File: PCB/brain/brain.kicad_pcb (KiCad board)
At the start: 4 copper layers, 100 x 115 mm, 225 parts, among them J1 Screw_Terminal_01x02, J10 Conn_01x12, J11 Conn_01x04, J12 BAT, J13 Conn_01x05, J14 Conn_01x02, J2 Conn_01x04, J3 RJ45_Hanrun_HR911105A_Horizon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, J4 Conn_01x04, J5 Conn_01x04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

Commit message: no DRC ERRORS
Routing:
- net Net-(Q1-D): track 8.29 -> 13.8 mm
- net VBUS: track 30.8 -> 36.0 mm
- net VS: track 47.5 -> 49.9 mm, vias 3 -> 4
- net GND: track 402.9 -> 400.7 mm, vias 218 -> 295
- net INTn: track 63.0 -> 64.9 mm
- net 5VHP_EN: track 56.7 -> 57.3 mm
- net VSYS: vias 30 -> 100
- net +5V: vias 23 -> 28
- added copper zone on In2.Cu, net +5V
- added copper zone on B.Cu, net Net-(Q1-D)
- added copper zone on F.Cu, net Net-(Q1-D)
- added copper zone on In2.Cu, net Net-(Q1-D)

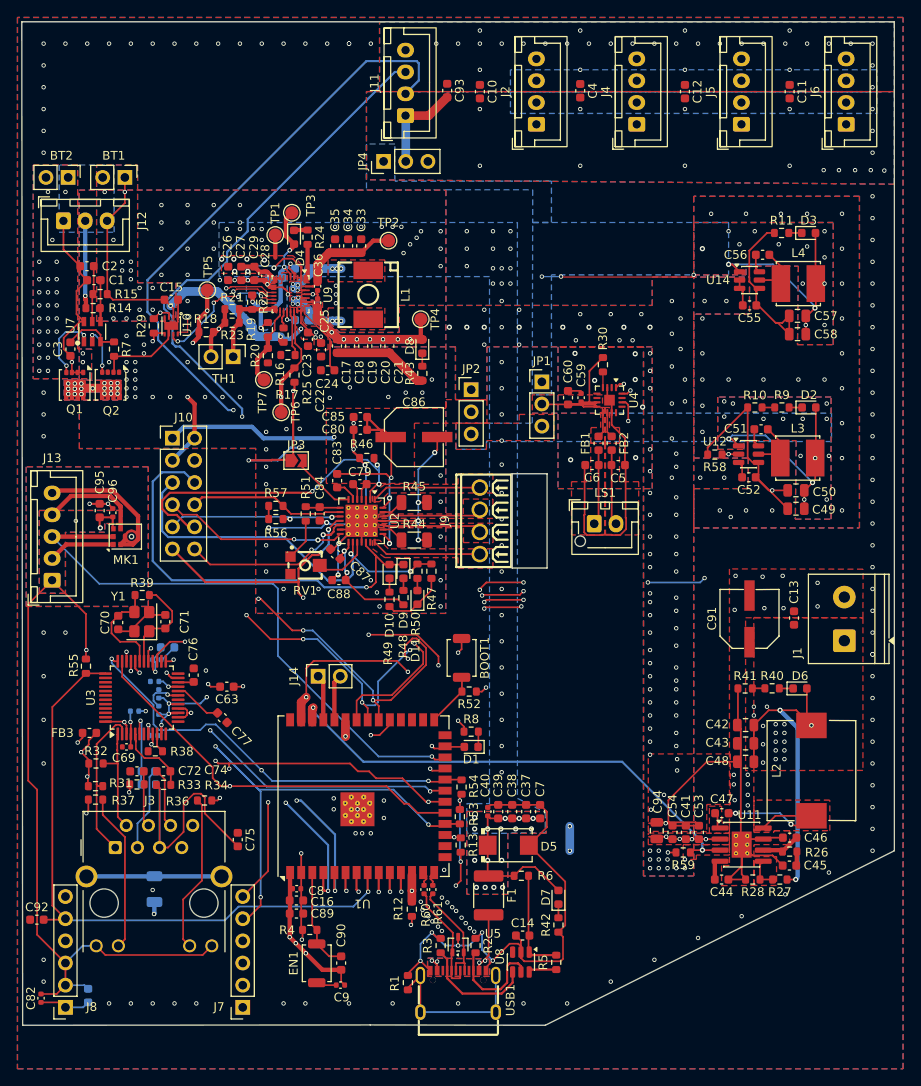
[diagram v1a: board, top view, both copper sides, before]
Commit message: no DRC important warnings
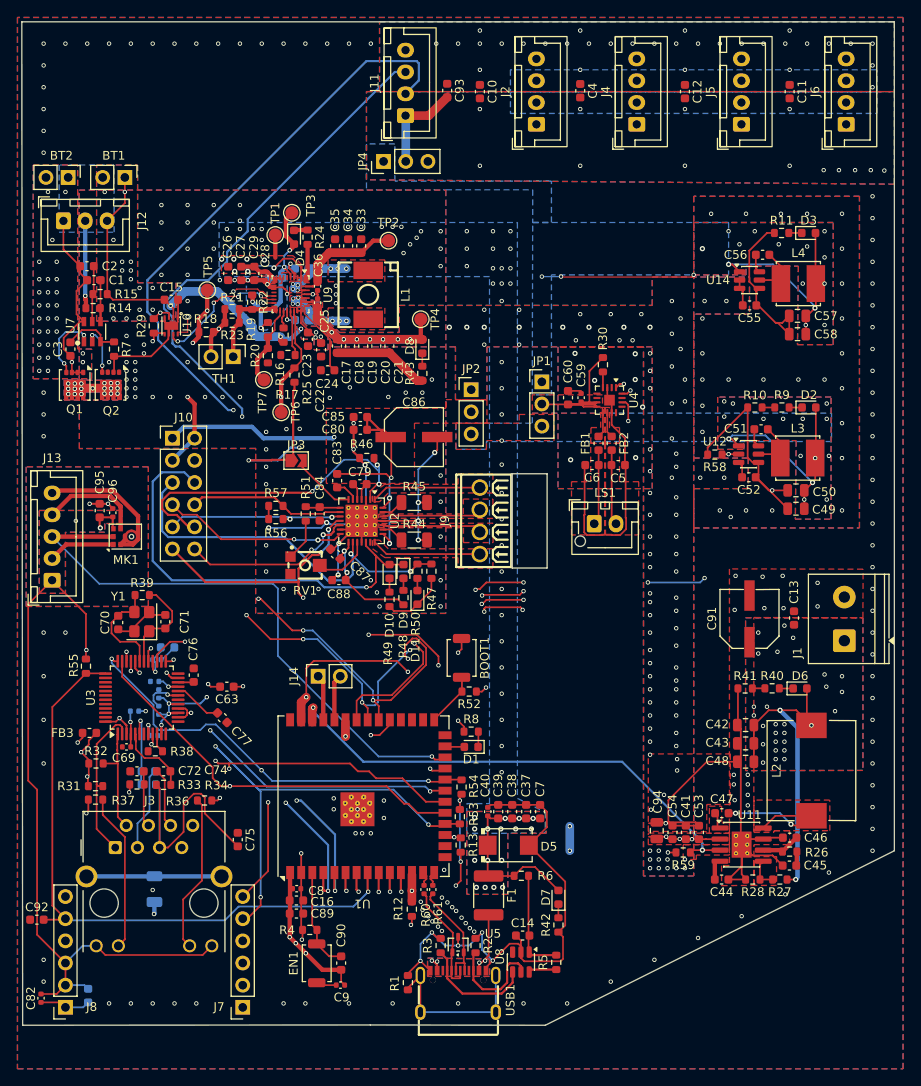
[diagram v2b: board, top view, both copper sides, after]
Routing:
- net QON: track 5.83 -> 0.00 mm, vias 1 -> 0
- net Net-(D1-A): track 3.91 -> 2.29 mm, vias 1 -> 0
- net /SW2: track 9.01 -> 9.61 mm
- net /SW1: track 7.95 -> 8.55 mm
- net GND: track 400.7 -> 401.3 mm, vias 295 -> 290
- net VSYS: vias 100 -> 98
- net SCLK: vias 4 -> 3
- net 5VHP: vias 19 -> 29
- net +3.3VA: vias 12 -> 11
- net +3.3V: vias 32 -> 31
- added copper zone on In2.Cu, net +BATT
- added copper zone on B.Cu, net 5VHP
- added copper zone on In2.Cu, net 5VHP

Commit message: make pcb fit into 100x100mm area
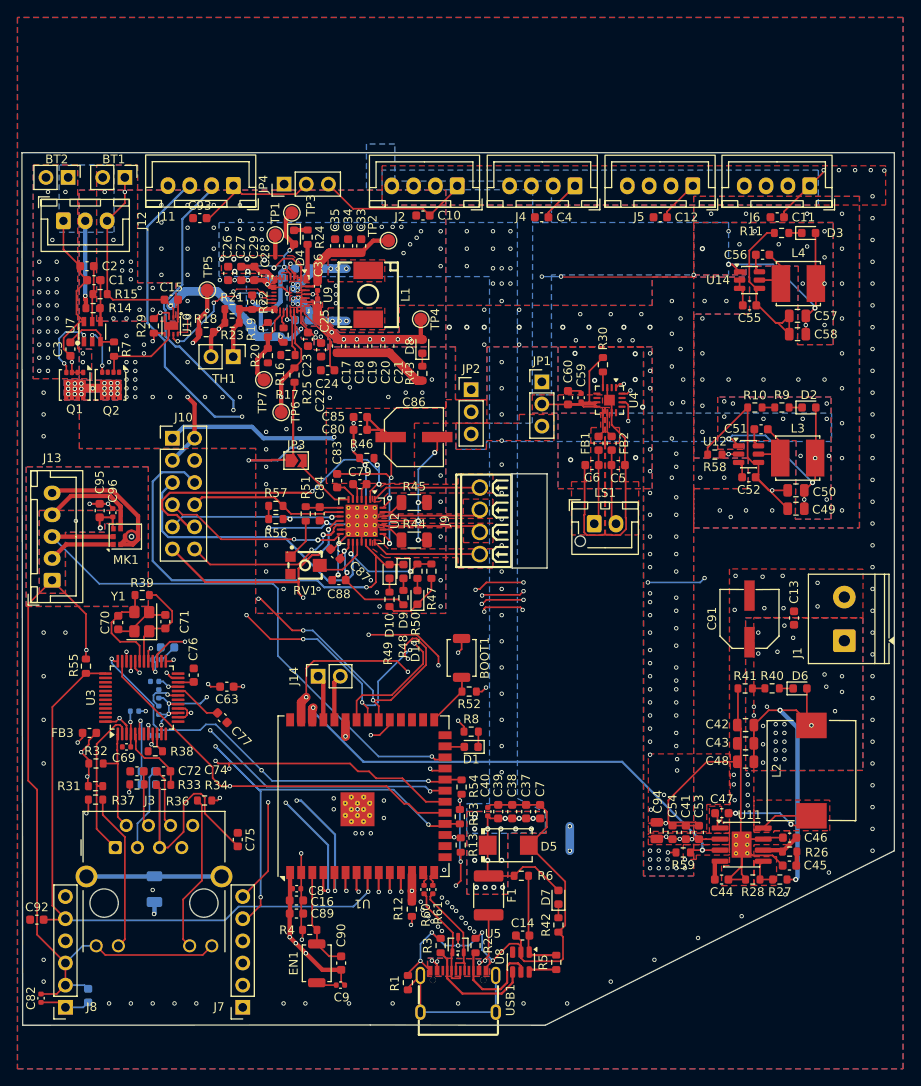
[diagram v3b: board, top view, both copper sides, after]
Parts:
- moved C93 31.9 mm to (70.4, 57.5), turned to 0 degrees
- moved J11 21.3 mm to (74.2, 53.8), turned to 180 degrees
- moved C10 15.6 mm to (96.0, 57.2), turned to 0 degrees
- moved C4 15.2 mm to (109.6, 57.4), turned to 0 degrees
- moved C12 14.7 mm to (123.2, 57.4), turned to 0 degrees
- moved C11 14.5 mm to (136.6, 57.4), turned to 0 degrees
- moved JP4 11.7 mm to (80.1, 53.6)
- moved J2 11.5 mm to (99.9, 53.8), turned to 180 degrees
- moved J4 9.99 mm to (113.4, 53.8), turned to 180 degrees
- moved J5 8.99 mm to (126.9, 53.8), turned to 180 degrees
- moved J6 8.19 mm to (140.3, 53.8), turned to 180 degrees
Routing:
- net SDA: track 177.0 -> 141.3 mm
- net +5V: track 25.6 -> 60.4 mm, vias 28 -> 20
- net RX1: track 127.1 -> 93.6 mm
- net TX1: track 118.3 -> 96.0 mm
- net SCL: track 183.7 -> 171.1 mm
- net Net-(J11-Pin_1): track 10.9 -> 14.4 mm
- net GND: vias 290 -> 237
- added copper zone on In2.Cu, net SDA
- removed copper zone on B.Cu, net SDA
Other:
- board size 100 x 115 mm -> 100 x 100 mm
